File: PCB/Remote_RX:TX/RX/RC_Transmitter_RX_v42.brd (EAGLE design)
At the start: 50 x 70 mm, 27 parts, among them IC1 LAMBDA80C-24S, IC4 ESP32-WROVER-IE-N16R8, J1 MOLEX_53261-0271MOLEX_53261-0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, SW1 KMR2, SW2 KMR2, U1 AP2112K-3.3TRG1SOT_RG1_DIO-L, U2 AP2112K-3.3TRG1SOT_RG1_DIO-L

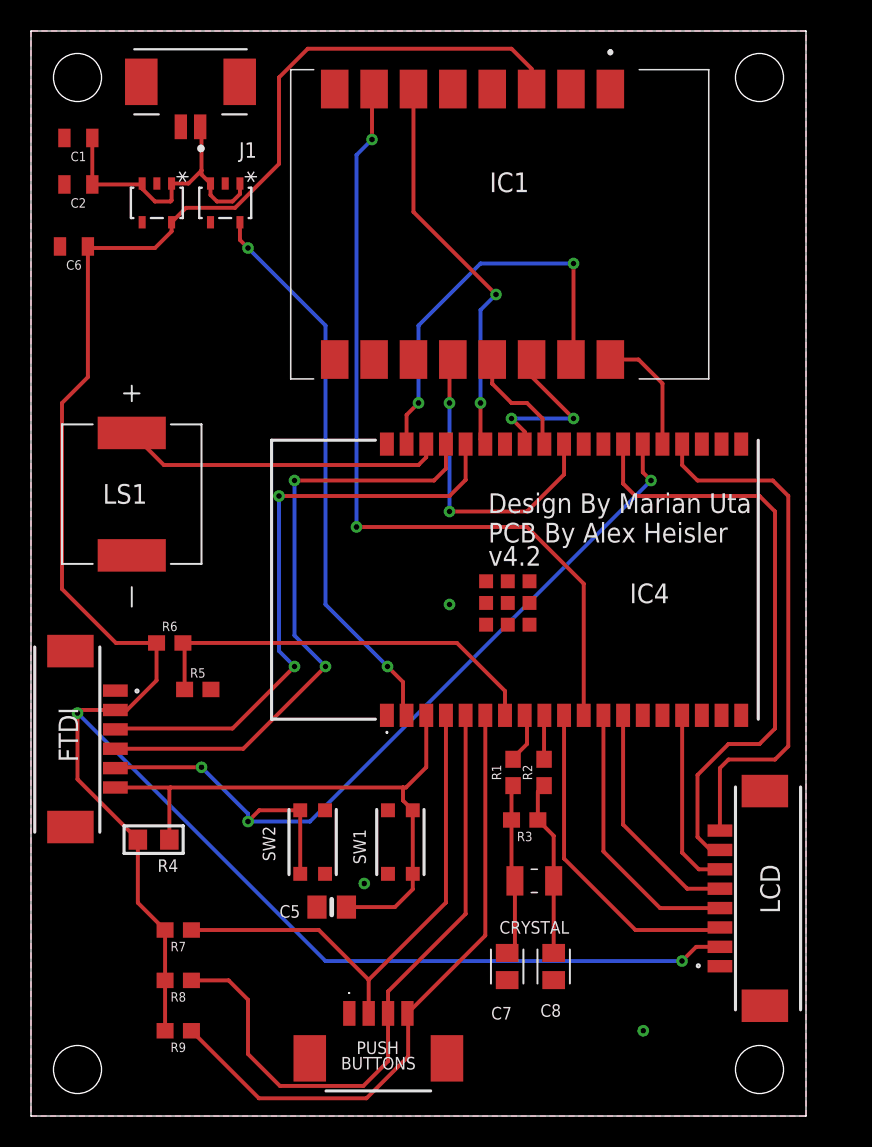
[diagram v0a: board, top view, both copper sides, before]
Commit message: Remote RX - PCB Update
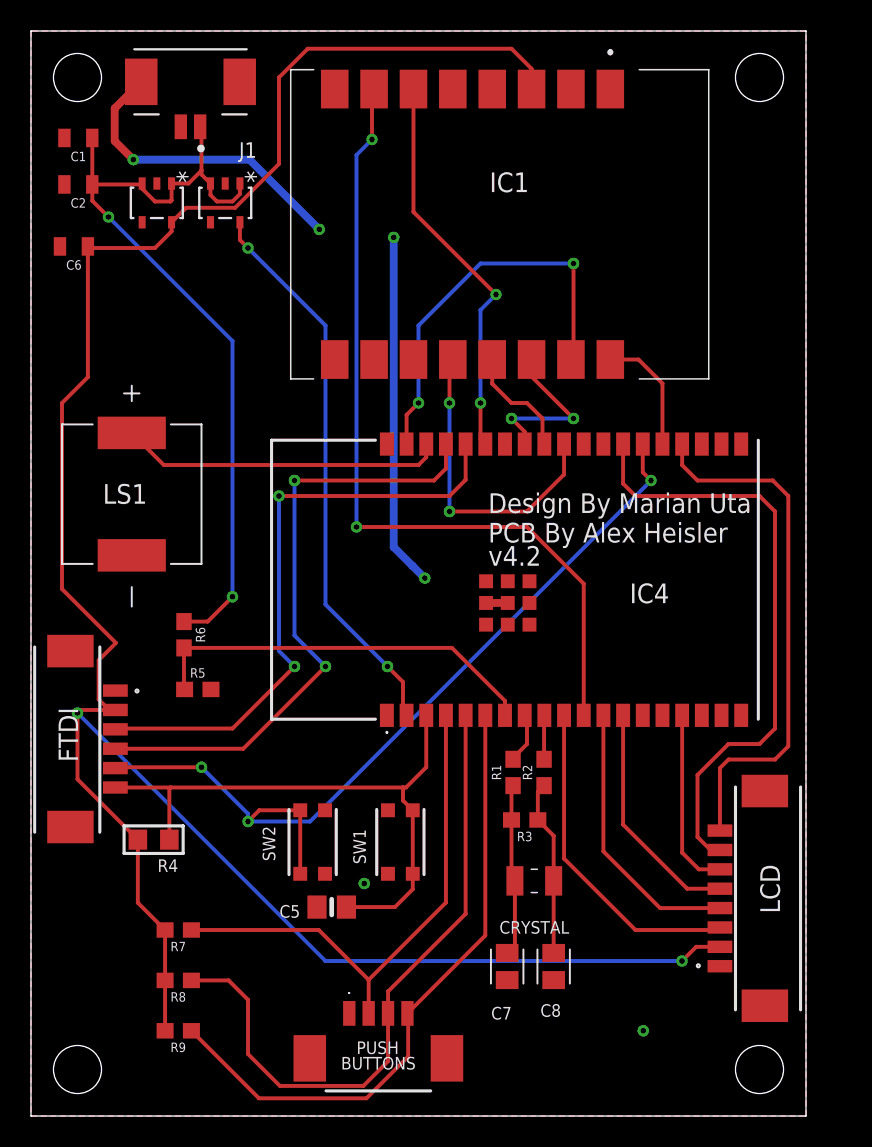
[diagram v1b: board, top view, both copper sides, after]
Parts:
- moved R6 1.06 mm to (9.87, 31.1), turned to 270 degrees
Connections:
- net 3.3V: no longer R6.1
- net VIN: now also R6.1
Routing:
- net GND: track 0.00 -> 44.3 mm, vias 3 -> 6
- net VIN: track 19.8 -> 54.0 mm, vias 0 -> 2
- net 3.3V: track 149.5 -> 146.4 mm
- net GPIO35*: track 26.7 -> 25.8 mm
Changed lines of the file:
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@@
 <setting verticaltext="up"/>
 </settings>
-<grid distance="0.5" unitdist="mm" unit="mm" style="lines" multiple="1" display="yes" altdistance="5" altunitdist="mil" altunit="mil"/>
+<grid distance="0.1" unitdist="mm" unit="mm" style="lines" multiple="1" display="yes" altdistance="2" altunitdist="mil" altunit="mil"/>
 <layers>
 <layer number="1" name="Top" color="4" fill="1" visible="yes" active="yes"/>
@@
 <attribute name="PROD_ID" value="RES-08609" x="26" y="-69" size="1.778" layer="27" display="off"/>
 </element>
-<element name="R6" library="SparkFun-Resistors" library_urn="urn:adsk.eagle:library:532" package="0603" package3d_urn="urn:adsk.eagle:package:39650/1" value="10k" x="8.95" y="30.52" smashed="yes">
-<attribute name="NAME" x="8.95" y="31.282" size="0.6096" layer="25" font="vector" ratio="20" align="bottom-center"/>
-<attribute name="PROD_ID" value="RES-08609" x="28" y="-66" size="1.778" layer="27" display="off"/>
+<element name="R6" library="SparkFun-Resistors" library_urn="urn:adsk.eagle:library:532" package="0603" package3d_urn="urn:adsk.eagle:package:39650/1" value="10k" x="9.87" y="31.05" smashed="yes" rot="R270">
+<attribute name="NAME" x="10.632" y="31.05" size="0.6096" layer="25" font="vector" ratio="20" rot="R270" align="bottom-center"/>
+<attribute name="PROD_ID" value="RES-08609" x="-86.65" y="12" size="1.778" layer="27" rot="R270" display="off"/>
 </element>
 <element name="SW1" library="microbuilder" package="BTN_KMR2_4.6X2.8" value="KMR2" x="23.83" y="17.675" smashed="yes" rot="R90">
@@
 <vertex x="0" y="70"/>
 </polygon>
-<via x="27" y="33" extent="1-16" drill="0.35"/>
 <via x="21.5" y="15" extent="1-16" drill="0.35"/>
 <via x="39.5" y="5.5" extent="1-16" drill="0.35"/>
-<wire x1="29.36" y1="33.1" x2="30.76" y2="33.1" width="0" layer="19" extent="1-1"/>
+<wire x1="7.115" y1="66.72" x2="5.4" y2="65.005" width="0.508" layer="1"/>
+<via x="18.6" y="57.2" extent="1-16" drill="0.35"/>
+<via x="6.6" y="61.7" extent="1-16" drill="0.35"/>
+<wire x1="6.6" y1="61.7" x2="14.1" y2="61.7" width="0.508" layer="16"/>
+<wire x1="14.1" y1="61.7" x2="18.6" y2="57.2" width="0.508" layer="16"/>
+<wire x1="6.6" y1="61.7" x2="5.4" y2="62.9" width="0.508" layer="1"/>
+<wire x1="5.4" y1="62.9" x2="5.4" y2="65.005" width="0.508" layer="1"/>
+<via x="23.4" y="56.6846" extent="1-16" drill="0.35"/>
+<wire x1="23.4" y1="56.6846" x2="23.4" y2="36.7" width="0.508" layer="16"/>
+<via x="25.4048" y="34.7048" extent="1-16" drill="0.35"/>
+<wire x1="23.4" y1="36.7" x2="24.6" y2="35.5" width="0.508" layer="16"/>
+<wire x1="24.6096" y1="35.5" x2="25.4048" y2="34.7048" width="0.508" layer="16"/>
+<wire x1="24.6" y1="35.5" x2="24.6096" y2="35.5" width="0.508" layer="16"/>
+<wire x1="29.36" y1="33.1" x2="30.76" y2="33.1" width="0.508" layer="1"/>
 </signal>
 <signal name="3.3V">
@@
 <contactref element="U2" pad="5"/>
 <contactref element="LCD" pad="2"/>
-<contactref element="R6" pad="1"/>
 <wire x1="44.446" y1="10.915" x2="42.915" y2="10.915" width="0.254" layer="1"/>
 <wire x1="42.915" y1="10.915" x2="42" y2="10" width="0.254" layer="1"/>
@@
 <wire x1="9.07" y1="57.659" x2="10.0046" y2="58.5936" width="0.254" layer="1"/>
 <wire x1="10.0046" y1="58.5936" x2="13.1683375" y2="58.5936" width="0.254" layer="1"/>
-<wire x1="5.444" y1="26.195" x2="6.195" y2="26.195" width="0.254" layer="1"/>
-<wire x1="8.1" y1="28.1" x2="8.1" y2="30.52" width="0.254" layer="1"/>
-<wire x1="6.195" y1="26.195" x2="8.1" y2="28.1" width="0.254" layer="1"/>
 <wire x1="16" y1="61.4252625" x2="16" y2="67" width="0.254" layer="1"/>
 <wire x1="16" y1="67" x2="17.857" y2="68.857" width="0.254" layer="1"/>
@@
 <wire x1="3.67" y1="56.1" x2="3.67" y2="47.67" width="0.254" layer="1"/>
 <wire x1="2" y1="34" x2="5.48" y2="30.52" width="0.254" layer="1"/>
-<wire x1="5.48" y1="30.52" x2="8.1" y2="30.52" width="0.254" layer="1"/>
 <wire x1="3.67" y1="47.67" x2="2" y2="46" width="0.254" layer="1"/>
 <wire x1="2" y1="46" x2="2" y2="34" width="0.254" layer="1"/>
@@
 <wire x1="8.65" y1="12" x2="6.894" y2="13.756" width="0.254" layer="1"/>
 <wire x1="6.894" y1="13.756" x2="6.894" y2="17.83" width="0.254" layer="1"/>
+<wire x1="5.48" y1="30.52" x2="4.364590625" y2="29.404590625" width="0.254" layer="1"/>
+<wire x1="4.364590625" y1="29.404590625" x2="4.364590625" y2="26.874409375" width="0.254" layer="1"/>
+<wire x1="4.364590625" y1="26.874409375" x2="5.044" y2="26.195" width="0.254" layer="1"/>
+<wire x1="5.044" y1="26.195" x2="5.444" y2="26.195" width="0.254" layer="1"/>
 </signal>
 <signal name="RXD">
@@
 <wire x1="7.109" y1="60.1" x2="3.955" y2="60.1" width="0.254" layer="1"/>
 <wire x1="3.955" y1="60.1" x2="3.955" y2="63.1" width="0.254" layer="1"/>
+<contactref element="R6" pad="1"/>
+<via x="13" y="33.5" extent="1-16" drill="0.35"/>
+<via x="5" y="58" extent="1-16" drill="0.35"/>
+<wire x1="5" y1="58" x2="13" y2="50" width="0.254" layer="16"/>
+<wire x1="13" y1="50" x2="13" y2="33.5" width="0.254" layer="16"/>
+<wire x1="3.955" y1="60.1" x2="3.955" y2="59.045" width="0.254" layer="1"/>
+<wire x1="3.955" y1="59.045" x2="5" y2="58" width="0.254" layer="1"/>
+<wire x1="13" y1="33.5" x2="11.4" y2="31.9" width="0.254" layer="1"/>
+<wire x1="9.87" y1="31.9" x2="11.4" y2="31.9" width="0.254" layer="1"/>
 </signal>
 <signal name="GPIO35*">
@@
 <contactref element="R5" pad="1"/>
 <contactref element="R6" pad="2"/>
-<wire x1="9.8" y1="30.52" x2="9.91" y2="30.41" width="0.254" layer="1"/>
-<wire x1="9.91" y1="30.41" x2="9.91" y2="27.52" width="0.254" layer="1"/>
-<wire x1="9.8" y1="30.52" x2="27.48" y2="30.52" width="0.254" layer="1"/>
-<wire x1="30.58" y1="27.42" x2="30.58" y2="25.85" width="0.254" layer="1"/>
-<wire x1="27.48" y1="30.52" x2="30.58" y2="27.42" width="0.254" layer="1"/>
+<wire x1="9.87" y1="30.2" x2="9.87" y2="27.56" width="0.254" layer="1"/>
+<wire x1="9.87" y1="27.56" x2="9.91" y2="27.52" width="0.254" layer="1"/>
+<wire x1="27.16" y1="30.2" x2="9.87" y2="30.2" width="0.254" layer="1"/>
+<wire x1="27.16" y1="30.2" x2="30.58" y2="26.78" width="0.254" layer="1"/>
+<wire x1="30.58" y1="26.78" x2="30.58" y2="25.85" width="0.254" layer="1"/>
 </signal>
 <signal name="3.3V*">
@@
 <via x="23" y="29" extent="1-16" drill="0.35"/>
 <wire x1="23" y1="29" x2="19" y2="33" width="0.254" layer="16"/>
-<wire x1="19" y1="51" x2="19" y2="33" width="0.254" layer="16"/>
+<wire x1="19" y1="33" x2="19" y2="51" width="0.254" layer="16"/>
 <wire x1="19" y1="51" x2="14" y2="56" width="0.254" layer="16"/>
 <via x="14" y="56" extent="1-16" drill="0.35"/>
